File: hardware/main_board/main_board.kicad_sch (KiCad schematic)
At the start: 83 parts, among them J1 USB_C_Receptacle_USB2.0_16P, J2 UART_DEBUG, J3 BAT1, J4 CTRL, J5 LED_CTRL, J6 HV_OUTPUT, Q1 MMBT3904, Q2 MMBT3904, SW1 SW_MEC_5G, U1 MPU-6050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

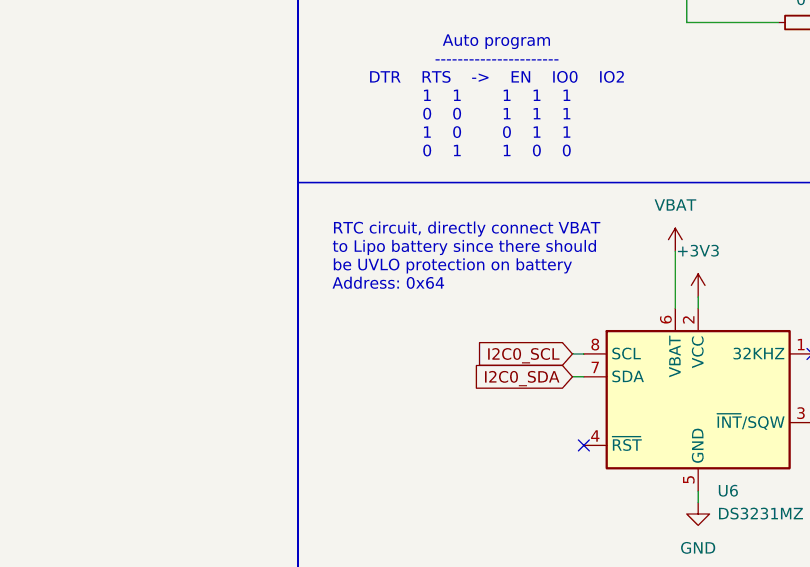
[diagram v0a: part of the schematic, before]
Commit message: fix(hardware): correct comment on schematic, change DZ3231 default address to 0x68
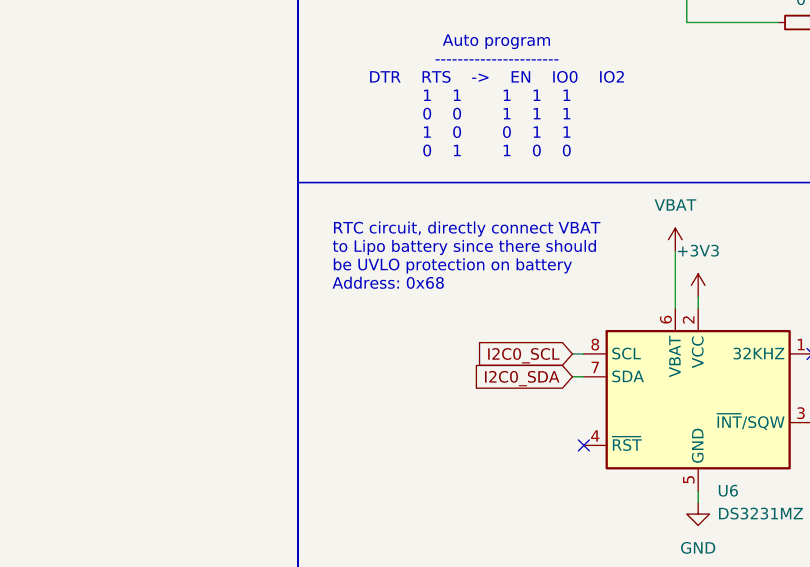
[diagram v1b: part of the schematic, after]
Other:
- note added: "RTC circuit, directly connect VBAT to Lipo battery since there should be UVLO protection on battery Address: 0x68"
- note removed: "RTC circuit, directly connect VBAT to Lipo battery since there should be UVLO protection on battery Address: 0x64"
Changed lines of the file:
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@@
 		)
 	)
-	(text "RTC circuit, directly connect VBAT \nto Lipo battery since there should\nbe UVLO protection on battery\nAddress: 0x64"
+	(text "RTC circuit, directly connect VBAT \nto Lipo battery since there should\nbe UVLO protection on battery\nAddress: 0x68"
 		(exclude_from_sim no)
 		(at 148.59 160.782 0)

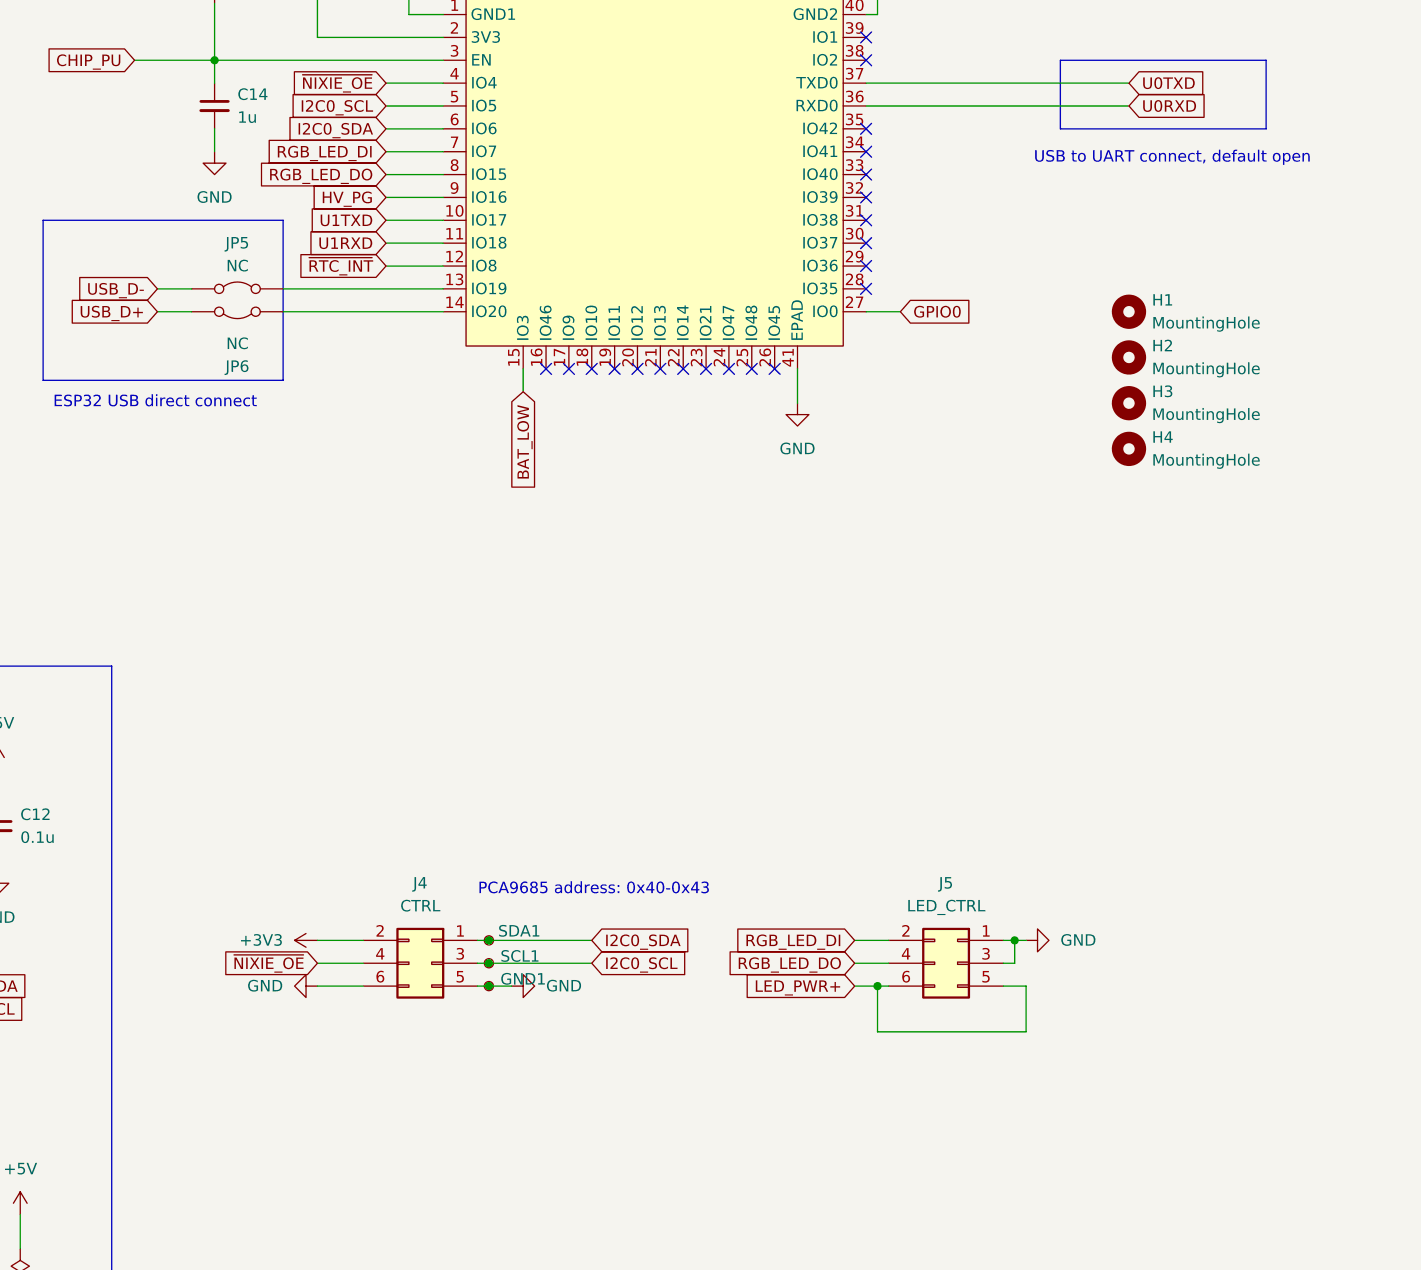
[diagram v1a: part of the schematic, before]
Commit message: hardware(sch): update hv boost output capacitor, update connector pinout
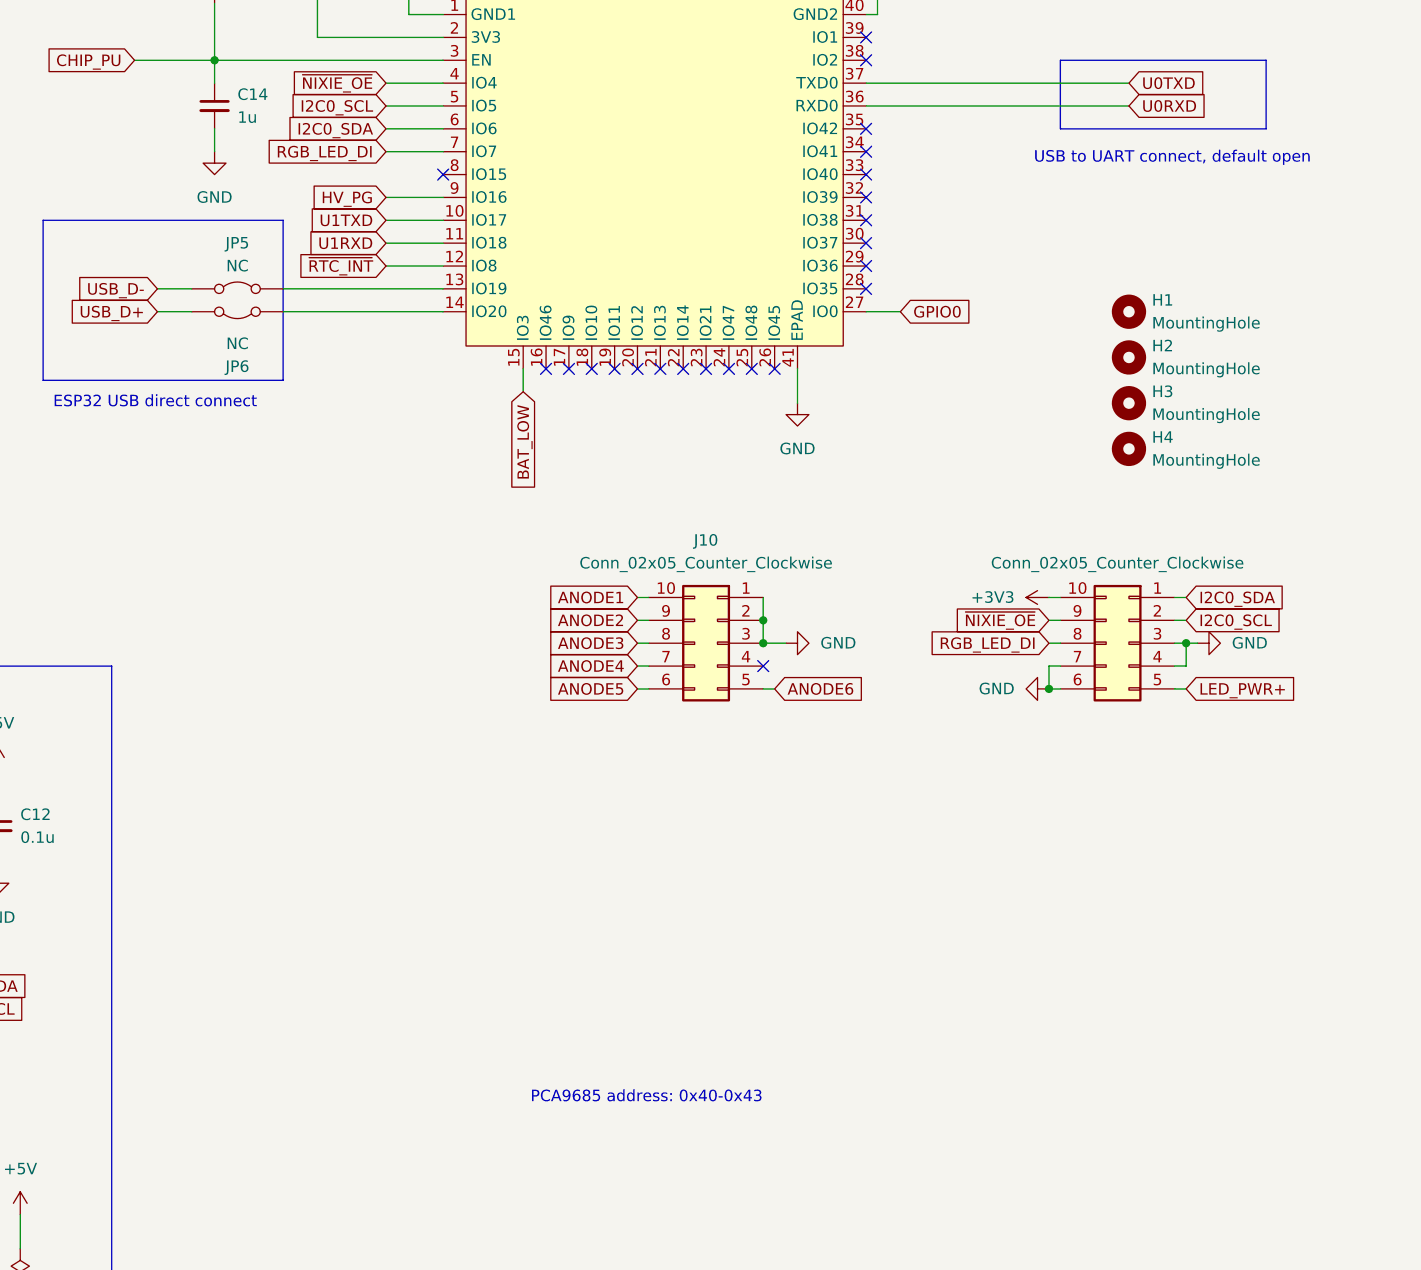
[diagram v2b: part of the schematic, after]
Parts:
- removed GND1: GND_TP, TestPoint:TestPoint_Pad_D2.0mm, symbol Connector:TestPoint_Small
- removed J4: CTRL, Connector_PinSocket_2.00mm:PinSocket_2x03_P2.00mm_Vertical, symbol Connector_Generic:Conn_02x03_Odd_Even
- removed J5: LED_CTRL, Connector_PinSocket_2.00mm:PinSocket_2x03_P2.00mm_Vertical, symbol Connector_Generic:Conn_02x03_Odd_Even
- removed SCL1: SCL_TP, TestPoint:TestPoint_Pad_D2.0mm, symbol Connector:TestPoint_Small
- removed SDA1: SDA_TP, TestPoint:TestPoint_Pad_D2.0mm, symbol Connector:TestPoint_Small
- added J10, J9: Conn_02x05_Counter_Clockwise, symbol Connector_Generic:Conn_02x05_Counter_Clockwise
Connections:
- net +3V3: now also J9.10 (Pin_10)
- net GND: now also J10.1 (Pin_1), J10.2 (Pin_2), J10.3 (Pin_3), J9.3 (Pin_3), J9.4 (Pin_4), J9.6 (Pin_6), J9.7 (Pin_7)
- net I2C0_SCL: now also J9.2 (Pin_2)
- net I2C0_SDA: now also J9.1 (Pin_1)
- net LED_PWR+: now also J9.5 (Pin_5)
- net RGB_LED_DI: now also J9.8 (Pin_8)
- net ~{NIXIE_OE}: now also J9.9 (Pin_9)
- net RGB_LED_DO: no longer names the net of U5.8 (IO15)
- new net ANODE1: J10.10 (Pin_10)
- new net ANODE2: J10.9 (Pin_9)
- new net ANODE3: J10.8 (Pin_8)
- new net ANODE4: J10.7 (Pin_7)
- new net ANODE5: J10.6 (Pin_6)
- new net ANODE6: J10.5 (Pin_5)
- no-connect marks 64 -> 66

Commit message: WIP(hardware): update in-4 display board
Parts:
- removed J6: HV_OUTPUT, Connector_PinSocket_2.00mm:PinSocket_2x03_P2.00mm_Vertical, symbol Connector_Generic:Conn_02x03_Odd_Even
- J10, J9: footprint (none) -> Connector_PinHeader_2.00mm:PinHeader_2x05_P2.00mm_Vertical
- J2: footprint Connector_PinHeader_2.54mm:PinHeader_1x04_P2.54mm_Horizontal -> Connector_PinHeader_2.00mm:PinHeader_1x04_P2.00mm_Horizontal

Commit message: WIP(hardware): in4 display board layout
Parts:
- removed J10, J9: Conn_02x05_Counter_Clockwise, Connector_PinHeader_2.00mm:PinHeader_2x05_P2.00mm_Vertical, symbol Connector_Generic:Conn_02x05_Counter_Clockwise
- added J4, J5: Conn_02x05_Odd_Even, Connector_PinHeader_2.00mm:PinHeader_2x05_P2.00mm_Vertical, symbol Connector_Generic:Conn_02x05_Odd_Even
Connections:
- net +3V3: now also J5.2 (Pin_2)
- net ANODE1: now also J4.2 (Pin_2)
- net ANODE2: now also J4.4 (Pin_4)
- net ANODE3: now also J4.6 (Pin_6)
- net ANODE4: now also J4.8 (Pin_8)
- net ANODE5: now also J4.10 (Pin_10)
- net ANODE6: now also J4.9 (Pin_9)
- net GND: now also J4.1 (Pin_1), J4.3 (Pin_3), J4.5 (Pin_5), J5.10 (Pin_10), J5.5 (Pin_5), J5.7 (Pin_7), J5.8 (Pin_8)
- net I2C0_SCL: now also J5.3 (Pin_3)
- net I2C0_SDA: now also J5.1 (Pin_1)
- net LED_PWR+: now also J5.9 (Pin_9)
- net RGB_LED_DI: now also J5.6 (Pin_6)
- net ~{NIXIE_OE}: now also J5.4 (Pin_4)
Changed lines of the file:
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@@
 	)
 	(junction
+		(at 332.74 193.04)
+		(diameter 0)
+		(color 0 0 0 0)
+	)
+	(junction
 		(at 151.13 55.88)
 		(diameter 0)
@@
 	)
 	(junction
-		(at 332.74 193.04)
-		(diameter 0)
-		(color 0 0 0 0)
-	)
-	(junction
 		(at 68.58 101.6)
 		(diameter 0)
@@
 	)
 	(junction
+		(at 332.74 195.58)
+		(diameter 0)
+		(color 0 0 0 0)
+	)
+	(junction
 		(at 66.04 210.82)
 		(diameter 0)
@@
 	)
 	(junction
-		(at 332.74 195.58)
-		(diameter 0)
-		(color 0 0 0 0)
-	)
-	(junction
 		(at 347.98 44.45)
 		(diameter 0)
@@
 	(wire
 		(pts
-			(xy 332.74 193.04) (xy 332.74 195.58)
+			(xy 332.74 190.5) (xy 332.74 193.04)
 		)
 		(stroke
@@
 	(wire
 		(pts
+			(xy 332.74 193.04) (xy 332.74 195.58)
+		)
+		(stroke
+			(width 0)
+			(type default)
+		)
+	)
+	(wire
+		(pts
 			(xy 133.35 222.25) (xy 130.81 222.25)
 		)
@@
 	(wire
 		(pts
-			(xy 332.74 190.5) (xy 332.74 193.04)
-		)
-		(stroke
-			(width 0)
-			(type default)
-		)
-	)
-	(wire
-		(pts
 			(xy 198.12 36.83) (xy 205.74 36.83)
 		)
@@
 	)
 	(symbol
+		(lib_id "Connector_Generic:Conn_02x05_Odd_Even")
+		(at 327.66 195.58 0)
+		(mirror y)
+		(unit 1)
+		(exclude_from_sim no)
+		(in_bom yes)
+		(on_board yes)
+		(dnp no)
+		(property "Reference" "J4"
+			(at 326.39 184.15 0)
+			(effects
+				(font
+					(size 1.27 1.27)
+				)
+			)
+		)
+		(property "Value" "Conn_02x05_Odd_Even"
+			(at 326.39 186.69 0)
+			(effects
+				(font
+					(size 1.27 1.27)
+				)
+			)
+		)
+		(property "Footprint" "Connector_PinHeader_2.00mm:PinHeader_2x05_P2.00mm_Vertical"
+			(at 327.66 195.58 0)
+			(effects
+				(font
+					(size 1.27 1.27)
+				)
+				(hide yes)
+			)
+		)
+		(property "Datasheet" "~"
+			(at 327.66 195.58 0)
+			(effects
+				(font
+					(size 1.27 1.27)
+				)
+				(hide yes)
+			)
+		)
+		(property "Description" "Generic connector, double row, 02x05, odd/even pin numbering scheme (row 1 odd numbers, row 2 even numbers), script generated (kicad-library-utils/schlib/autogen/connector/)"
+			(at 327.66 195.58 0)
+			(effects
+				(font
+					(size 1.27 1.27)
+				)
+				(hide yes)
+			)
+		)
+		(pin "10"
+		)
+		(pin "2"
+		)
+		(pin "3"
+		)
+		(pin "1"
+		)
+		(pin "9"
+		)
+		(pin "4"
+		)
+		(pin "8"
+		)
+		(pin "5"
+		)
+		(pin "7"
+		)
+		(pin "6"
+		)
+		(instances
+			(project ""
+				(path "/62950e93-3f98-4dee-9256-8213caa98ee7"
+					(reference "J4")
+					(unit 1)
+				)
+			)
+		)
+	)
+	(symbol
 		(lib_id "Device:C_Small")
 		(at 40.386 115.824 0)
@@
 	)
 	(symbol
-		(lib_id "Connector_Generic:Conn_02x05_Counter_Clockwise")
-		(at 327.66 195.58 0)
-		(mirror y)
-		(unit 1)
-		(exclude_from_sim no)
-		(in_bom yes)
-		(on_board yes)
-		(dnp no)
-		(property "Reference" "J10"
-			(at 326.39 184.15 0)
-			(effects
-				(font
-					(size 1.27 1.27)
-				)
-			)
-		)
-		(property "Value" "Conn_02x05_Counter_Clockwise"
-			(at 326.39 186.69 0)
-			(effects
-				(font
-					(size 1.27 1.27)
-				)
-			)
-		)
-		(property "Footprint" "Connector_PinHeader_2.00mm:PinHeader_2x05_P2.00mm_Vertical"
-			(at 327.66 195.58 0)
-			(effects
-				(font
-					(size 1.27 1.27)
-				)
-				(hide yes)
-			)
-		)
-		(property "Datasheet" "~"
-			(at 327.66 195.58 0)
-			(effects
-				(font
-					(size 1.27 1.27)
-				)
-				(hide yes)
-			)
-		)
-		(property "Description" "Generic connector, double row, 02x05, counter clockwise pin numbering scheme (similar to DIP package numbering), script generated (kicad-library-utils/schlib/autogen/connector/)"
-			(at 327.66 195.58 0)
-			(effects
-				(font
-					(size 1.27 1.27)
-				)
-				(hide yes)
-			)
-		)
-		(pin "1"
-		)
-		(pin "4"
-		)
-		(pin "8"
-		)
-		(pin "9"
-		)
-		(pin "3"
-		)
-		(pin "7"
-		)
-		(pin "5"
-		)
-		(pin "10"
-		)
-		(pin "2"
-		)
-		(pin "6"
-		)
-		(instances
-			(project "main_board"
-				(path "/62950e93-3f98-4dee-9256-8213caa98ee7"
-					(reference "J10")
-					(unit 1)
-				)
-			)
-		)
-	)
-	(symbol
 		(lib_id "Device:C_Small")
 		(at 222.25 77.47 0)
@@
 	)
 	(symbol
-		(lib_id "power:GND")
-		(at 115.57 222.25 0)
+		(lib_id "Connector_Generic:Conn_02x05_Odd_Even")
+		(at 373.38 195.58 0)
+		(mirror y)
 		(unit 1)
 		(exclude_from_sim no)
@@
 		(on_board yes)
 		(dnp no)
-		(fields_autoplaced yes)
-		(property "Reference" "#PWR017"
-			(at 115.57 228.6 0)
+		(property "Reference" "J5"
+			(at 372.11 184.15 0)
 			(effects
 				(font
 					(size 1.27 1.27)
 				)
-				(hide yes)
 			)
 		)
-		(property "Value" "GND"
-			(at 115.57 227.33 0)
+		(property "Value" "Conn_02x05_Odd_Even"
+			(at 372.11 186.69 0)
 			(effects
 				(font
@@
 			)
 		)
-		(property "Footprint" ""
-			(at 115.57 222.25 0)
+		(property "Footprint" "Connector_PinHeader_2.00mm:PinHeader_2x05_P2.00mm_Vertical"
+			(at 373.38 195.58 0)
 			(effects
 				(font
@@
 			)
 		)
-		(property "Datasheet" ""
-			(at 115.57 222.25 0)
+		(property "Datasheet" "~"
+			(at 373.38 195.58 0)
 			(effects
 				(font
@@
 			)
 		)
-		(property "Description" "Power symbol creates a global label with name \"GND\" , ground"
-			(at 115.57 222.25 0)
+		(property "Description" "Generic connector, double row, 02x05, odd/even pin numbering scheme (row 1 odd numbers, row 2 even numbers), script generated (kicad-library-utils/schlib/autogen/connector/)"
+			(at 373.38 195.58 0)
 			(effects
 				(font
@@
 			)
 		)
+		(pin "10"
+		)
+		(pin "2"
+		)
+		(pin "3"
+		)
 		(pin "1"
 		)
+		(pin "9"
+		)
+		(pin "4"
+		)
+		(pin "8"
+		)
+		(pin "5"
+		)
+		(pin "7"
+		)
+		(pin "6"
+		)
 		(instances
 			(project "main_board"
 				(path "/62950e93-3f98-4dee-9256-8213caa98ee7"
-					(reference "#PWR017")
+					(reference "J5")
 					(unit 1)
 				)
@@
 	(symbol
 		(lib_id "power:GND")
-		(at 345.44 121.92 180)
+		(at 115.57 222.25 0)
 		(unit 1)
 		(exclude_from_sim no)
@@
 		(dnp no)
 		(fields_autoplaced yes)
-		(property "Reference" "#PWR051"
-			(at 345.44 115.57 0)
+		(property "Reference" "#PWR017"
+			(at 115.57 228.6 0)
 			(effects
 				(font
@@
 		)
 		(property "Value" "GND"
-			(at 345.44 116.84 0)
+			(at 115.57 227.33 0)
 			(effects
 				(font
@@
 		)
 		(property "Footprint" ""
-			(at 345.44 121.92 0)
+			(at 115.57 222.25 0)
 			(effects
 				(font
@@
 		)
 		(property "Datasheet" ""
-			(at 345.44 121.92 0)
+			(at 115.57 222.25 0)
 			(effects
 				(font
@@
 		)
 		(property "Description" "Power symbol creates a global label with name \"GND\" , ground"
-			(at 345.44 121.92 0)
+			(at 115.57 222.25 0)
 			(effects
 				(font
@@
 			(project "main_board"
 				(path "/62950e93-3f98-4dee-9256-8213caa98ee7"
-					(reference "#PWR051")
+					(reference "#PWR017")
 					(unit 1)
 				)
@@
 	)
 	(symbol
-		(lib_id "Connector_Generic:Conn_02x05_Counter_Clockwise")
-		(at 373.38 195.58 0)
-		(mirror y)
+		(lib_id "power:GND")
+		(at 345.44 121.92 180)
 		(unit 1)
 		(exclude_from_sim no)
@@
 		(on_board yes)
 		(dnp no)
-		(property "Reference" "J9"
-			(at 372.11 184.15 0)
+		(fields_autoplaced yes)
+		(property "Reference" "#PWR051"
+			(at 345.44 115.57 0)
 			(effects
 				(font
@@
 			)
 		)
-		(property "Value" "Conn_02x05_Counter_Clockwise"
-			(at 372.11 186.69 0)
+		(property "Value" "GND"
+			(at 345.44 116.84 0)
 			(effects
 				(font
@@
 			)
 		)
-		(property "Footprint" "Connector_PinHeader_2.00mm:PinHeader_2x05_P2.00mm_Vertical"
-			(at 373.38 195.58 0)
+		(property "Footprint" ""
+			(at 345.44 121.92 0)
 			(effects
 				(font
@@
 			)
 		)
-		(property "Datasheet" "~"
-			(at 373.38 195.58 0)
+		(property "Datasheet" ""
+			(at 345.44 121.92 0)
 			(effects
 				(font
@@
 			)
 		)
-		(property "Description" "Generic connector, double row, 02x05, counter clockwise pin numbering scheme (similar to DIP package numbering), script generated (kicad-library-utils/schlib/autogen/connector/)"
-			(at 373.38 195.58 0)
+		(property "Description" "Power symbol creates a global label with name \"GND\" , ground"
+			(at 345.44 121.92 0)
 			(effects
 				(font
@@
 		(pin "1"
 		)
-		(pin "4"
-		)
-		(pin "8"
-		)
-		(pin "9"
-		)
-		(pin "3"
-		)
-		(pin "7"
-		)
-		(pin "5"
-		)
-		(pin "10"
-		)
-		(pin "2"
-		)
-		(pin "6"
-		)
 		(instances
 			(project "main_board"
 				(path "/62950e93-3f98-4dee-9256-8213caa98ee7"
-					(reference "J9")
+					(reference "#PWR051")
 					(unit 1)
 				)
